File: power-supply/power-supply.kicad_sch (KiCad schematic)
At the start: 15 parts, among them J101 CUI_PD-30, P101 IEC_60320_C13_Plug, SW101 SW_DPST_x2, T101 Transformer_1P_2S

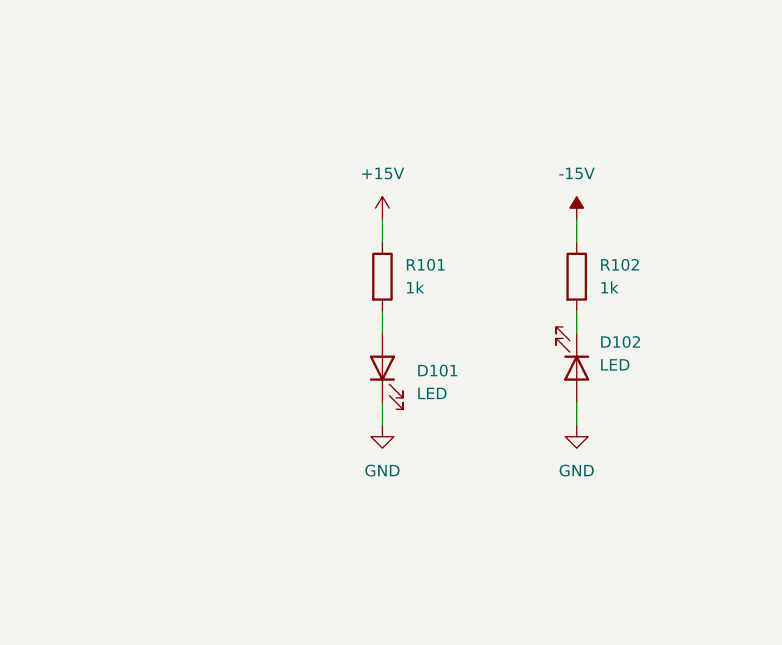
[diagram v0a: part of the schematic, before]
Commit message: Some additions to power supply
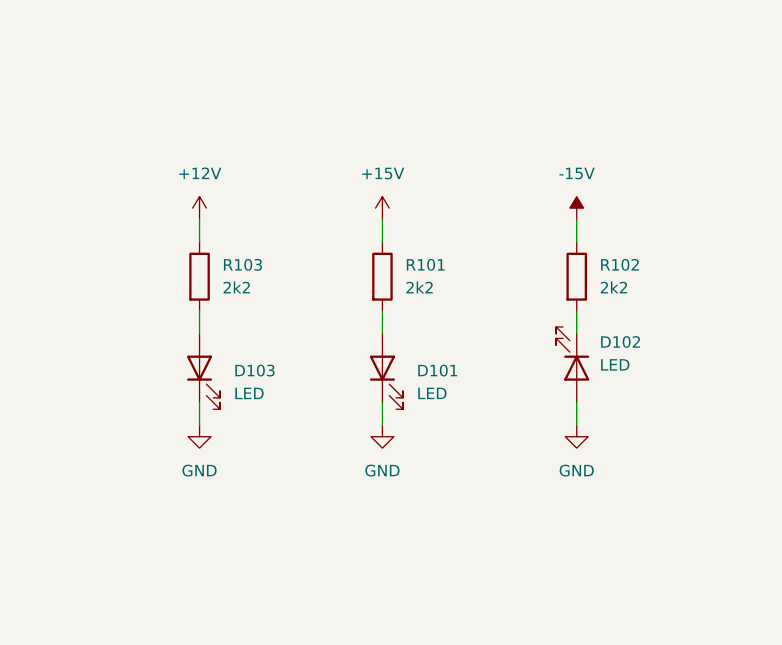
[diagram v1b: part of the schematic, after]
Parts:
- added D103: LED, LED_THT:LED_D5.0mm_Horizontal_O3.81mm_Z3.0mm, symbol Device:LED
- added R103: 2k2, Resistor_THT:R_Axial_DIN0207_L6.3mm_D2.5mm_P10.16mm_Horizontal, symbol Device:R
- R101, R102: value 1k -> 2k2
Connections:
- net GND: now also D103.1 (K)
- new net: D103.2 (A), R103.2
- new net +12V: R103.1
